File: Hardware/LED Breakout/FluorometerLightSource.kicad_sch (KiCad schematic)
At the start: 5 parts

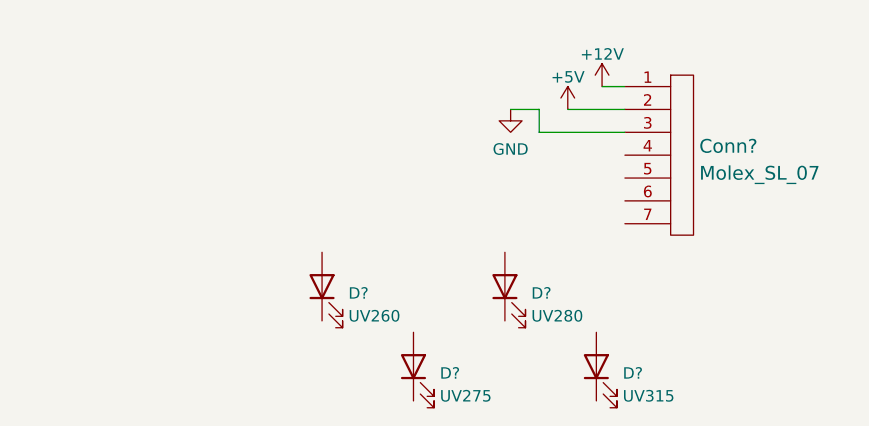
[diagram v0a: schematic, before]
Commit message: LED Resistor Values
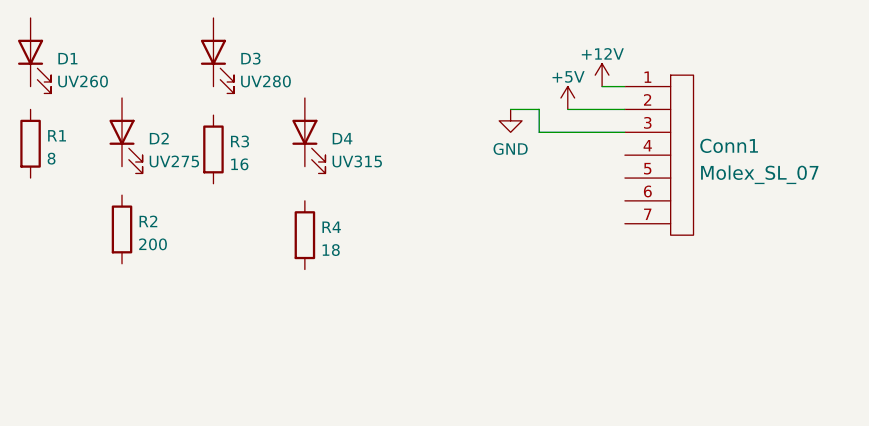
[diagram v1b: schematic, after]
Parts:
- added R1: 8, symbol Device:R
- added R2: 200, symbol Device:R
- added R3: 16, symbol Device:R
- added R4: 18, symbol Device:R
- gave numbers to parts that had none: 5
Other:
- moved on the sheet: D1, D2, D3, D4

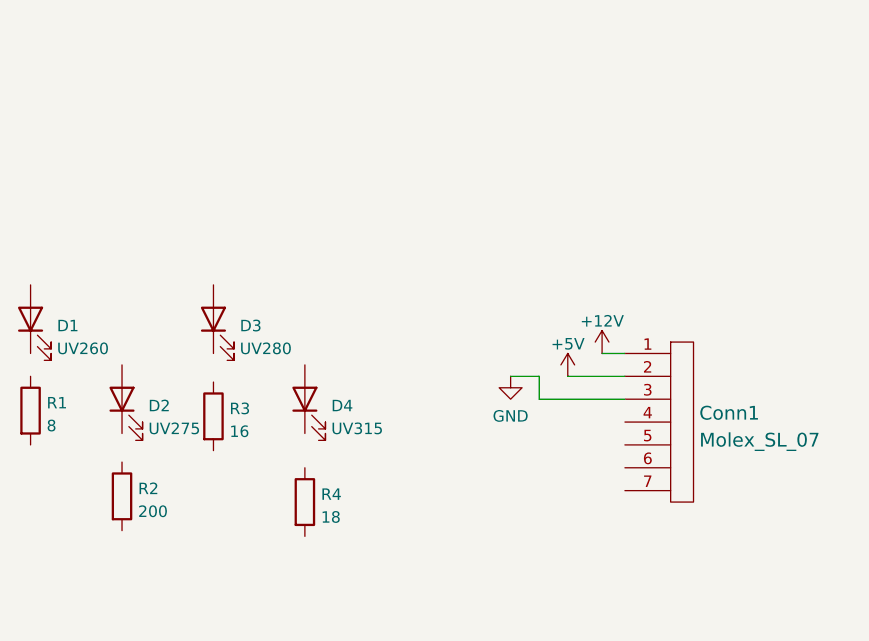
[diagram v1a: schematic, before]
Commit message: NH3, LED Mosfets
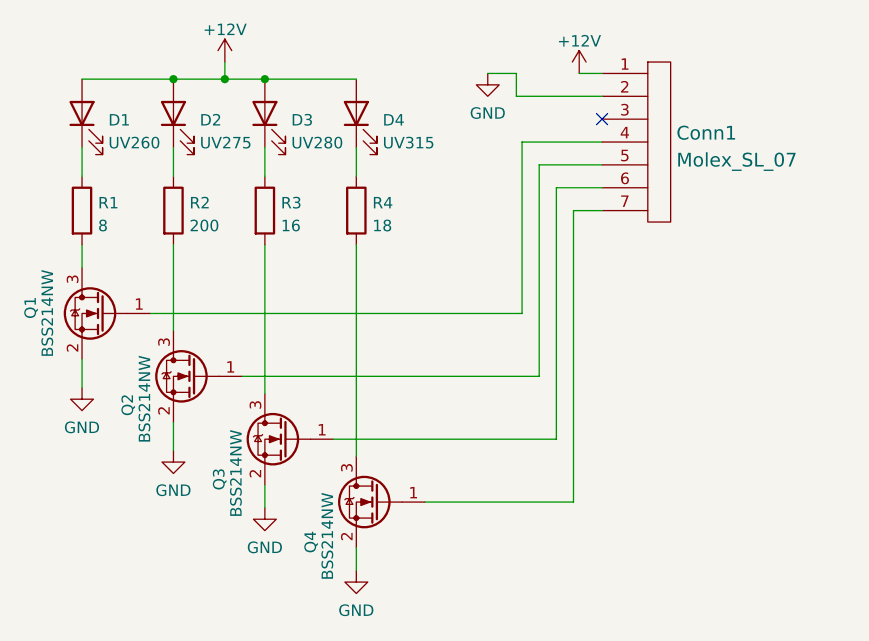
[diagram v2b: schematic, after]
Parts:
- added Q1, Q2, Q3, Q4: BSS214NW, Package_TO_SOT_SMD:SOT-323_SC-70, symbol Transistor_FET:BSS214NW
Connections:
- net +5V is gone; now on net GND: Conn1.2
- net +12V: now also D1.2 (A), D2.2 (A), D3.2 (A), D4.2 (A)
- net GND: now also Q1.2 (S), Q2.2 (S), Q3.2 (S), Q4.2 (S); no longer Conn1.3
- net at R2.1: now also D2.1 (K)
- net at R2.2: now also Q2.3 (D)
- net at D1.1 (K): now also R1.1
- net at R4.1: now also D4.1 (K)
- net at R4.2: now also Q4.3 (D)
- net at Conn1.4: now also Q1.1 (G)
- net at Conn1.5: now also Q2.1 (G)
- net at Conn1.6: now also Q3.1 (G)
- net at Conn1.7: now also Q4.1 (G)
- net at R1.2: now also Q1.3 (D)
- net at D3.1 (K): now also R3.1
- net at R3.2: now also Q3.3 (D)
- no-connect marks 0 -> 1
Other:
- moved on the sheet: Conn1, D1, D2, D3, D4, R1, R2, R3, R4

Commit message: Footprint Assignment
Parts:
- Conn1: footprint (none) -> MRDT_Connectors:MOLEX_SL_07_Horizontal
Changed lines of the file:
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@@
       (effects (font (size 1.524 1.524)) (justify left))
     )
-    (property "Footprint" "" (id 2) (at 215.265 35.56 0)
+    (property "Footprint" "MRDT_Connectors:MOLEX_SL_07_Horizontal" (id 2) (at 215.265 35.56 0)
       (effects (font (size 1.524 1.524)) hide)
     )
@@
     )
     (path "/52110cb2-5608-431d-a2bc-c6332c172407"
-      (reference "Conn1") (unit 1) (value "Molex_SL_07") (footprint "")
+      (reference "Conn1") (unit 1) (value "Molex_SL_07") (footprint "MRDT_Connectors:MOLEX_SL_07_Horizontal")
     )
     (path "/2738bbfd-5112-4f65-9482-13e7a539d128"

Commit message: Footprints added in paths
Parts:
- D1: footprint (none) -> UVLEDs:KL26550USMWD
- D2: footprint (none) -> UVLEDs:SUCULBN1VCAGAY674F4G30R18
- D3: footprint (none) -> UVLEDs:XBT3535UVA130CD27501
- D4: footprint (none) -> UVLEDs:WS3535C48LF-310
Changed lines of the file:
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@@
       (effects (font (size 1.27 1.27)) (justify right))
     )
-    (property "Footprint" "" (id 2) (at 152.4 28.575 0)
+    (property "Footprint" "UVLEDs:KL26550USMWD" (id 2) (at 152.4 28.575 0)
       (effects (font (size 1.27 1.27)) hide)
     )
@@
       (effects (font (size 1.27 1.27)) (justify right))
     )
-    (property "Footprint" "" (id 2) (at 182.88 28.575 0)
+    (property "Footprint" "UVLEDs:WS3535C48LF-310" (id 2) (at 182.88 28.575 0)
       (effects (font (size 1.27 1.27)) hide)
     )
@@
       (effects (font (size 1.27 1.27)) (justify right))
     )
-    (property "Footprint" "" (id 2) (at 172.72 28.575 0)
+    (property "Footprint" "UVLEDs:XBT3535UVA130CD27501" (id 2) (at 172.72 28.575 0)
       (effects (font (size 1.27 1.27)) hide)
     )
@@
       (effects (font (size 1.27 1.27)) (justify right))
     )
-    (property "Footprint" "" (id 2) (at 162.56 28.575 0)
+    (property "Footprint" "UVLEDs:SUCULBN1VCAGAY674F4G30R18" (id 2) (at 162.56 28.575 0)
       (effects (font (size 1.27 1.27)) hide)
     )
@@
     )
     (path "/2738bbfd-5112-4f65-9482-13e7a539d128"
-      (reference "D1") (unit 1) (value "UV260") (footprint "")
+      (reference "D1") (unit 1) (value "UV260") (footprint "UVLEDs:KL26550USMWD")
     )
     (path "/b64cbaa3-3efc-4389-8802-370241ca5fbe"
-      (reference "D2") (unit 1) (value "UV275") (footprint "")
+      (reference "D2") (unit 1) (value "UV275") (footprint "UVLEDs:SUCULBN1VCAGAY674F4G30R18")
     )
     (path "/98df8fa6-a939-42be-9344-874a3277a644"
-      (reference "D3") (unit 1) (value "UV280") (footprint "")
+      (reference "D3") (unit 1) (value "UV280") (footprint "UVLEDs:XBT3535UVA130CD27501")
     )
     (path "/66b4715f-30a5-4530-bec7-c312163ca6c5"
-      (reference "D4") (unit 1) (value "UV315") (footprint "")
+      (reference "D4") (unit 1) (value "UV315") (footprint "UVLEDs:WS3535C48LF-310")
     )
     (path "/687f57a0-1afc-4cc0-a6d8-2c6ed5c8804c"

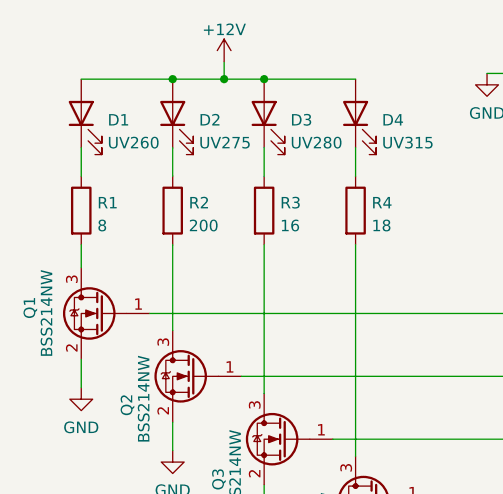
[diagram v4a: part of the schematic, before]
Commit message: Mosfets & H-Bridge Organized, Photodiode organized, Footprints for LED
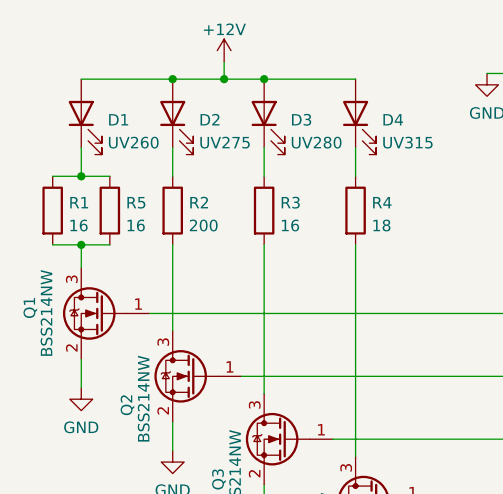
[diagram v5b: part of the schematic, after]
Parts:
- added R5: 16, Resistor_SMD:R_2512_6332Metric_Pad1.40x3.35mm_HandSolder, symbol Device:R
- R1: value 8 -> 16; footprint (none) -> Resistor_SMD:R_2512_6332Metric_Pad1.40x3.35mm_HandSolder
- R2: footprint (none) -> Resistor_SMD:R_0603_1608Metric_Pad0.98x0.95mm_HandSolder
- R3, R4: footprint (none) -> Resistor_SMD:R_2512_6332Metric_Pad1.40x3.35mm_HandSolder
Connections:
- net at D1.1 (K), R1.1: now also R5.1
- net at Q1.3 (D), R1.2: now also R5.2
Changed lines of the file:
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@@
   (junction (at 168.275 24.765) (diameter 0) (color 0 0 0 0)
   )
+  (junction (at 152.4 43.18) (diameter 0) (color 0 0 0 0)
+  )
   (junction (at 162.56 24.765) (diameter 0) (color 0 0 0 0)
+  )
+  (junction (at 152.4 35.56) (diameter 0) (color 0 0 0 0)
   )
   (junction (at 172.72 24.765) (diameter 0) (color 0 0 0 0)
@@
     (stroke (width 0) (type default) (color 0 0 0 0))
   )
+  (wire (pts (xy 152.4 35.56) (xy 155.575 35.56))
+    (stroke (width 0) (type default) (color 0 0 0 0))
+  )
   (wire (pts (xy 168.275 24.765) (xy 172.72 24.765))
     (stroke (width 0) (type default) (color 0 0 0 0))
@@
     (stroke (width 0) (type default) (color 0 0 0 0))
   )
+  (wire (pts (xy 149.225 35.56) (xy 152.4 35.56))
+    (stroke (width 0) (type default) (color 0 0 0 0))
+  )
   (wire (pts (xy 162.56 62.865) (xy 162.56 66.04))
     (stroke (width 0) (type default) (color 0 0 0 0))
@@
     (stroke (width 0) (type default) (color 0 0 0 0))
   )
+  (wire (pts (xy 149.225 43.18) (xy 152.4 43.18))
+    (stroke (width 0) (type default) (color 0 0 0 0))
+  )
   (wire (pts (xy 205.105 64.77) (xy 180.34 64.77))
     (stroke (width 0) (type default) (color 0 0 0 0))
@@
     (stroke (width 0) (type default) (color 0 0 0 0))
   )
+  (wire (pts (xy 152.4 43.18) (xy 155.575 43.18))
+    (stroke (width 0) (type default) (color 0 0 0 0))
+  )
   (wire (pts (xy 162.56 32.385) (xy 162.56 35.56))
     (stroke (width 0) (type default) (color 0 0 0 0))
@@
       (effects (font (size 1.27 1.27)) (justify left))
     )
-    (property "Footprint" "" (id 2) (at 160.782 39.37 90)
+    (property "Footprint" "Resistor_SMD:R_0603_1608Metric_Pad0.98x0.95mm_HandSolder" (id 2) (at 160.782 39.37 90)
       (effects (font (size 1.27 1.27)) hide)
     )
@@
       (effects (font (size 1.27 1.27)) (justify left))
     )
-    (property "Footprint" "" (id 2) (at 181.102 39.37 90)
+    (property "Footprint" "Resistor_SMD:R_2512_6332Metric_Pad1.40x3.35mm_HandSolder" (id 2) (at 181.102 39.37 90)
       (effects (font (size 1.27 1.27)) hide)
     )
@@
     )
     (pin "1")
+  )
+  (symbol (lib_id "Device:R") (at 155.575 39.37 0) (unit 1)
+    (in_bom yes) (on_board yes) (fields_autoplaced)
+    (property "Reference" "R5" (id 0) (at 157.353 38.5353 0)
+      (effects (font (size 1.27 1.27)) (justify left))
+    )
+    (property "Value" "16" (id 1) (at 157.353 41.0722 0)
+      (effects (font (size 1.27 1.27)) (justify left))
+    )
+    (property "Footprint" "Resistor_SMD:R_2512_6332Metric_Pad1.40x3.35mm_HandSolder" (id 2) (at 153.797 39.37 90)
+      (effects (font (size 1.27 1.27)) hide)
+    )
+    (property "Datasheet" "~" (id 3) (at 155.575 39.37 0)
+      (effects (font (size 1.27 1.27)) hide)
+    )
+    (pin "1")
+    (pin "2")
   )
   (symbol (lib_id "MRDT_Connectors:Molex_SL_07") (at 215.265 40.64 0) (unit 1)
@@
     (pin "3")
   )
-  (symbol (lib_id "Device:R") (at 152.4 39.37 0) (unit 1)
-    (in_bom yes) (on_board yes) (fields_autoplaced)
-    (property "Reference" "R1" (id 0) (at 154.178 38.5353 0)
-      (effects (font (size 1.27 1.27)) (justify left))
-    )
-    (property "Value" "8" (id 1) (at 154.178 41.0722 0)
-      (effects (font (size 1.27 1.27)) (justify left))
-    )
-    (property "Footprint" "" (id 2) (at 150.622 39.37 90)
-      (effects (font (size 1.27 1.27)) hide)
-    )
-    (property "Datasheet" "~" (id 3) (at 152.4 39.37 0)
+  (symbol (lib_id "Device:R") (at 149.225 39.37 0) (unit 1)
+    (in_bom yes) (on_board yes) (fields_autoplaced)
+    (property "Reference" "R1" (id 0) (at 151.003 38.5353 0)
+      (effects (font (size 1.27 1.27)) (justify left))
+    )
+    (property "Value" "16" (id 1) (at 151.003 41.0722 0)
+      (effects (font (size 1.27 1.27)) (justify left))
+    )
+    (property "Footprint" "Resistor_SMD:R_2512_6332Metric_Pad1.40x3.35mm_HandSolder" (id 2) (at 147.447 39.37 90)
+      (effects (font (size 1.27 1.27)) hide)
+    )
+    (property "Datasheet" "~" (id 3) (at 149.225 39.37 0)
       (effects (font (size 1.27 1.27)) hide)
     )
@@
       (effects (font (size 1.27 1.27)) (justify left))
     )
-    (property "Footprint" "" (id 2) (at 170.942 39.37 90)
+    (property "Footprint" "Resistor_SMD:R_2512_6332Metric_Pad1.40x3.35mm_HandSolder" (id 2) (at 170.942 39.37 90)
       (effects (font (size 1.27 1.27)) hide)
     )
@@
       (reference "Q4") (unit 1) (value "BSS214NW") (footprint "Package_TO_SOT_SMD:SOT-323_SC-70")
     )
-    (path "/7bdc2227-bfad-4b09-9a3b-cf441ac658ac"
-      (reference "R1") (unit 1) (value "8") (footprint "")
+    (path "/767c1b93-de91-4468-a9e8-f726948c2aa9"
+      (reference "R1") (unit 1) (value "16") (footprint "Resistor_SMD:R_2512_6332Metric_Pad1.40x3.35mm_HandSolder")
     )
     (path "/13fca39a-711d-4460-874c-e2058c5d59ed"
-      (reference "R2") (unit 1) (value "200") (footprint "")
+      (reference "R2") (unit 1) (value "200") (footprint "Resistor_SMD:R_0603_1608Metric_Pad0.98x0.95mm_HandSolder")
     )
     (path "/e30e3b2b-59a6-443f-86ec-c55e04f16be1"
-      (reference "R3") (unit 1) (value "16") (footprint "")
+      (reference "R3") (unit 1) (value "16") (footprint "Resistor_SMD:R_2512_6332Metric_Pad1.40x3.35mm_HandSolder")
     )
     (path "/342fb729-253f-4e0a-9da1-2d1f6ce188fe"
-      (reference "R4") (unit 1) (value "18") (footprint "")
-    )
-  )
+      (reference "R4") (unit 1) (value "18") (footprint "Resistor_SMD:R_2512_6332Metric_Pad1.40x3.35mm_HandSolder")
+    )
+    (path "/4dbc500a-5ffb-4f09-a085-b7c5d2bf958a"
+      (reference "R5") (unit 1) (value "16") (footprint "Resistor_SMD:R_2512_6332Metric_Pad1.40x3.35mm_HandSolder")
+    )
+  )

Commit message: Breakout Boards
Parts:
- added V1, V2, V3, V4: Via, MRDT_Drill_Holes:4_40_Hole, symbol MRDT_Drill_Holes:Via
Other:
- note added: "LEDs"
- note added: "Vias"
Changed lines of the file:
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@@
     (stroke (width 0) (type default) (color 0 0 0 0))
+  )
+  (text "LEDs" (at 172.72 94.615 0)
+    (effects (font (size 4 4)) (justify left bottom))
+  )
+  (text "Vias" (at 102.235 48.26 0)
+    (effects (font (size 4 4)) (justify left bottom))
   )
   (symbol (lib_id "Device:R") (at 162.56 39.37 0) (unit 1)
@@
     (pin "1")
   )
+  (symbol (lib_id "MRDT_Drill_Holes:Via") (at 113.03 26.67 0) (unit 1)
+    (in_bom yes) (on_board yes)
+    (property "Reference" "V3" (id 0) (at 118.8212 25.1968 0)
+      (effects (font (size 1.524 1.524)) (justify left))
+    )
+    (property "Value" "Via" (id 1) (at 118.8212 27.8892 0)
+      (effects (font (size 1.524 1.524)) (justify left))
+    )
+    (property "Footprint" "MRDT_Drill_Holes:4_40_Hole" (id 2) (at 113.03 26.67 0)
+      (effects (font (size 1.524 1.524)) hide)
+    )
+    (property "Datasheet" "" (id 3) (at 113.03 26.67 0)
+      (effects (font (size 1.524 1.524)) hide)
+    )
+    (pin "1")
+  )
   (symbol (lib_id "power:+12V") (at 168.275 22.86 0) (unit 1)
     (in_bom yes) (on_board yes) (fields_autoplaced)
@@
     (pin "3")
   )
+  (symbol (lib_id "MRDT_Drill_Holes:Via") (at 95.885 26.67 0) (unit 1)
+    (in_bom yes) (on_board yes)
+    (property "Reference" "V1" (id 0) (at 101.6762 25.1968 0)
+      (effects (font (size 1.524 1.524)) (justify left))
+    )
+    (property "Value" "Via" (id 1) (at 101.6762 27.8892 0)
+      (effects (font (size 1.524 1.524)) (justify left))
+    )
+    (property "Footprint" "MRDT_Drill_Holes:4_40_Hole" (id 2) (at 95.885 26.67 0)
+      (effects (font (size 1.524 1.524)) hide)
+    )
+    (property "Datasheet" "" (id 3) (at 95.885 26.67 0)
+      (effects (font (size 1.524 1.524)) hide)
+    )
+    (pin "1")
+  )
   (symbol (lib_id "Device:R") (at 172.72 39.37 0) (unit 1)
     (in_bom yes) (on_board yes) (fields_autoplaced)
@@
     (pin "1")
     (pin "2")
+  )
+  (symbol (lib_id "MRDT_Drill_Holes:Via") (at 95.885 34.29 0) (unit 1)
+    (in_bom yes) (on_board yes)
+    (property "Reference" "V2" (id 0) (at 101.6762 32.8168 0)
+      (effects (font (size 1.524 1.524)) (justify left))
+    )
+    (property "Value" "Via" (id 1) (at 101.6762 35.5092 0)
+      (effects (font (size 1.524 1.524)) (justify left))
+    )
+    (property "Footprint" "MRDT_Drill_Holes:4_40_Hole" (id 2) (at 95.885 34.29 0)
+      (effects (font (size 1.524 1.524)) hide)
+    )
+    (property "Datasheet" "" (id 3) (at 95.885 34.29 0)
+      (effects (font (size 1.524 1.524)) hide)
+    )
+    (pin "1")
+  )
+  (symbol (lib_id "MRDT_Drill_Holes:Via") (at 113.03 34.29 0) (unit 1)
+    (in_bom yes) (on_board yes)
+    (property "Reference" "V4" (id 0) (at 118.8212 32.8168 0)
+      (effects (font (size 1.524 1.524)) (justify left))
+    )
+    (property "Value" "Via" (id 1) (at 118.8212 35.5092 0)
+      (effects (font (size 1.524 1.524)) (justify left))
+    )
+    (property "Footprint" "MRDT_Drill_Holes:4_40_Hole" (id 2) (at 113.03 34.29 0)
+      (effects (font (size 1.524 1.524)) hide)
+    )
+    (property "Datasheet" "" (id 3) (at 113.03 34.29 0)
+      (effects (font (size 1.524 1.524)) hide)
+    )
+    (pin "1")
   )
   (symbol (lib_id "power:GND") (at 172.72 72.39 0) (unit 1)
@@
       (reference "R5") (unit 1) (value "16") (footprint "Resistor_SMD:R_2512_6332Metric_Pad1.40x3.35mm_HandSolder")
     )
-  )
+    (path "/e2bebf65-aa26-4019-84ad-d61424889fca"
+      (reference "V1") (unit 1) (value "Via") (footprint "MRDT_Drill_Holes:4_40_Hole")
+    )
+    (path "/ebcb7a93-3aeb-4d3f-ad60-1c95c4e3e677"
+      (reference "V2") (unit 1) (value "Via") (footprint "MRDT_Drill_Holes:4_40_Hole")
+    )
+    (path "/8866f183-99f3-452a-9c4b-da7029d6028d"
+      (reference "V3") (unit 1) (value "Via") (footprint "MRDT_Drill_Holes:4_40_Hole")
+    )
+    (path "/f6d29890-400f-413e-8276-4326f6261049"
+      (reference "V4") (unit 1) (value "Via") (footprint "MRDT_Drill_Holes:4_40_Hole")
+    )
+  )

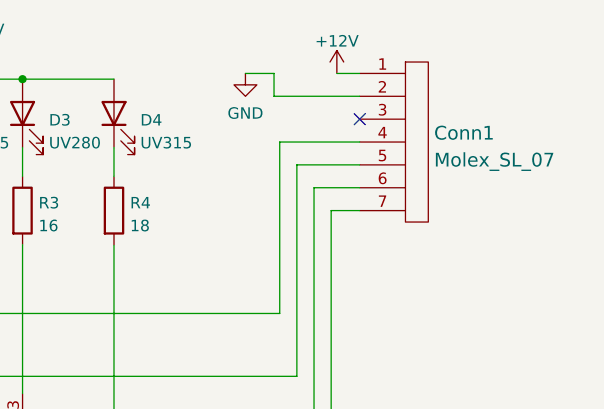
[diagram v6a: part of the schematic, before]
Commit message: Changed MolexSL7 on LED breakout to SL6
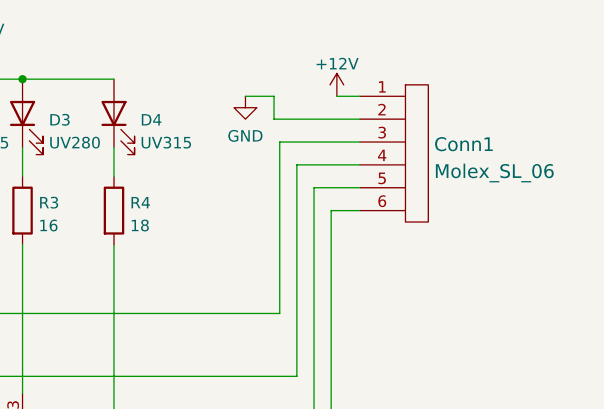
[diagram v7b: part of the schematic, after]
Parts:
- removed Conn1: Molex_SL_07, MRDT_Connectors:MOLEX_SL_07_Horizontal, symbol MRDT_Connectors:Molex_SL_07
- added Conn1: Molex_SL_06, UVLEDs:705550040, symbol Molex_SL_06:Molex_SL_06
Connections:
- net +12V: now also Conn1.1
- net GND: now also Conn1.2
- net at Q1.1 (G): now also Conn1.3
- net at Q2.1 (G): now also Conn1.4
- net at Q3.1 (G): now also Conn1.5
- net at Q4.1 (G): now also Conn1.6
- no-connect marks 1 -> 0

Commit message: CCD, LED changes
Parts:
- added D5: UV315, UVLEDs:WS3535C48LF-310, symbol Device:LED
- added D6: UV280, UVLEDs:XBT3535UVA130CD27501, symbol Device:LED
- added D7: UV275, UVLEDs:SUCULBN1VCAGAY674F4G30R18, symbol Device:LED
- added D8: UV260, UVLEDs:KL26550USMWD, symbol Device:LED
- added Q5, Q6, Q7, Q8: BSS214NW, Package_TO_SOT_SMD:SOT-323_SC-70, symbol Transistor_FET:BSS214NW
- added R10, R7, R9: 16, Resistor_SMD:R_2512_6332Metric_Pad1.40x3.35mm_HandSolder, symbol Device:R
- added R6: 18, Resistor_SMD:R_2512_6332Metric_Pad1.40x3.35mm_HandSolder, symbol Device:R
- added R8: 200, Resistor_SMD:R_0603_1608Metric_Pad0.98x0.95mm_HandSolder, symbol Device:R
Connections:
- net +12V: now also D5.2 (A), D6.2 (A), D7.2 (A), D8.2 (A)
- net GND: now also Q5.2 (S), Q6.2 (S), Q7.2 (S), Q8.2 (S)
- net at Conn1.3, Q1.1 (G): now also Q8.1 (G)
- net at Conn1.6, Q4.1 (G): now also Q5.1 (G)
- net at Conn1.4, Q2.1 (G): now also Q7.1 (G)
- net at Conn1.5, Q3.1 (G): now also Q6.1 (G)
- new net: D6.1 (K), R7.1
- new net: Q6.3 (D), R7.2
- new net: Q7.3 (D), R8.2
- new net: D8.1 (K), R10.1, R9.1
- new net: Q8.3 (D), R10.2, R9.2
- new net: Q5.3 (D), R6.2
- new net: D5.1 (K), R6.1
- new net: D7.1 (K), R8.1
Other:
- moved on the sheet: Conn1, V1, V2, V3, V4
